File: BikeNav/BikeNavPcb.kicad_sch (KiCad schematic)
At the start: 3 parts, among them U1 TP4056, U2 ESP32-C3_SUPERMINI_TH

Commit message: Update PCB Design
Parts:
- added C1: 0.1 µF, Capacitor_THT:C_Disc_D10.0mm_W2.5mm_P5.00mm, symbol Device:C
- added J9: 1.8 TFT SPi 128x160 pins, Connector_PinSocket_2.54mm:PinSocket_1x08_P2.54mm_Vertical, symbol Connector:Conn_01x08_Pin
- added R1, R2: 100k, Resistor_THT:R_Axial_DIN0204_L3.6mm_D1.6mm_P5.08mm_Horizontal, symbol Device:R_US
- added SW1: SW_DPST_x2, Button_Switch_SMD:SW_DIP_SPSTx01_Slide_Copal_CHS-01A_W5.08mm_P1.27mm_JPin, symbol Switch:SW_DPST_x2
- added U3: 358, ST7735:ST7735, symbol ST7735:358
- U1: footprint Footprint:TP4056 -> TP4056:TP4056
- U2: footprint ESP32-C3_SUPERMINI_TH:MODULE_ESP32-C3_SUPERMINI_TH -> ESP32C3_Supermini_symbol_footprint:MODULE_ESP32-C3_SUPERMINI_TH
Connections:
- net BACKLIGHT: now also J9.1 (Pin_1), U3.1 (LITE)
- net OUT+: now also J9.8 (Pin_8), R1.2, SW1.2 (B), U3.9 (VCC); no longer U1.3 (OUT+)
- net OUT-: now also J9.7 (Pin_7), R2.2, U3.10 (GND)
- net BATT EST: now reaches U2.0 (GPIO0)
- net BATT EST: now also C1.1, R1.1
- net A0: now reaches U2.2 (GPIO2)
- net A0: now also J9.4 (Pin_4), U3.7 (D/C)
- net RESET: now reaches U2.3 (GPIO3)
- net RESET: now also J9.5 (Pin_5), U3.8 (RESET)
- net SCK: now reaches U2.4 (GPIO4)
- net SCK: now also J9.2 (Pin_2), U3.3 (SCK)
- net SDA: now reaches U2.6 (GPIO6)
- net SDA: now also J9.3 (Pin_3), U3.4 (MOSI)
- net CS: now reaches U2.7 (GPIO7)
- net CS: now also J9.6 (Pin_6), U3.5 (TFT_CS)
- new net: SW1.1 (A), U1.3 (OUT+)
- new net: C1.2, R2.1
- no-connect marks 0 -> 9
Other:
- note added: "1.8 TFT SPI 128*160 Display"
- note added: "Battery Charge Estimation Voltage Divider Circuit"
- note added: "Li ion Battery Charger and MCU Supply Voltage"
- note added: "Microcontroller unit"
- note added: "TFT Display Horizontal Pins Connector"
- moved on the sheet: BT1, U1, U2

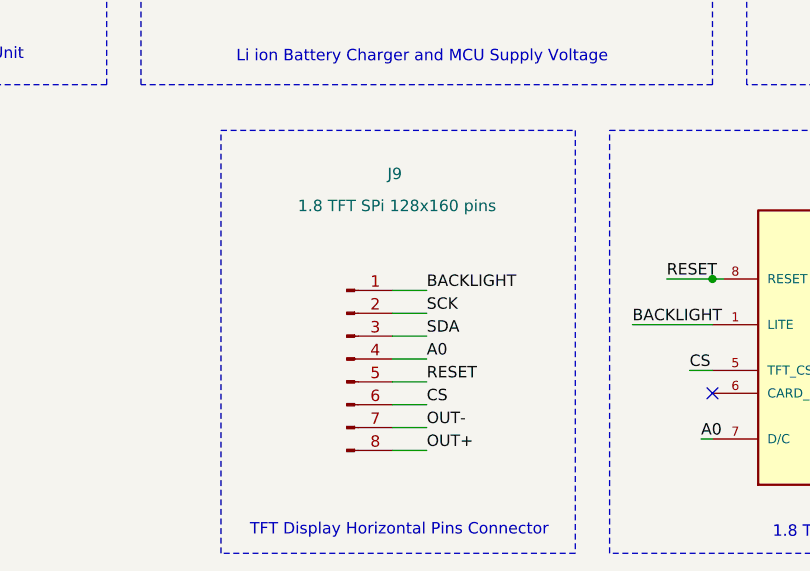
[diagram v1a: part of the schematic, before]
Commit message: Added Accurate dimesnsions for TFT mounting Holes and general optimization for Route Tracks.
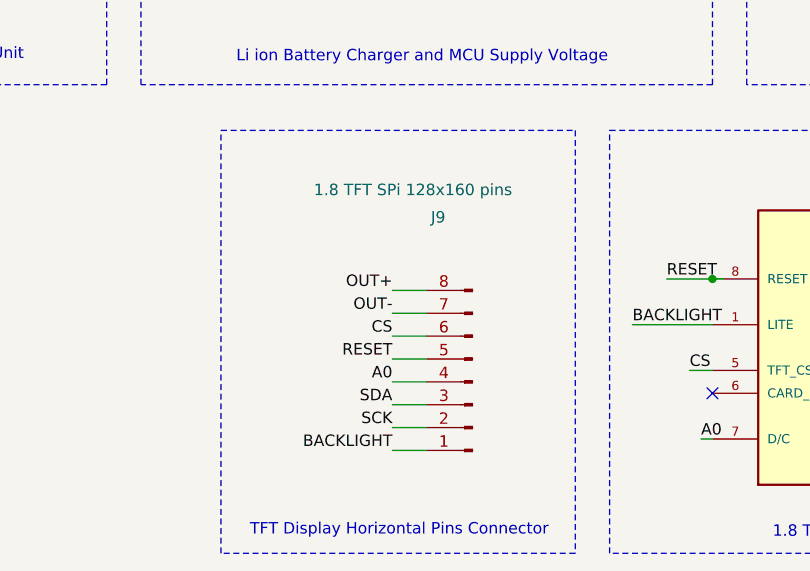
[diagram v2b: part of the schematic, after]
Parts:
- J9: footprint Connector_PinSocket_2.54mm:PinSocket_1x08_P2.54mm_Vertical -> Connector_PinHeader_2.54mm:PinHeader_1x08_P2.54mm_Vertical
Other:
- moved on the sheet: J9
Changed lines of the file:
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@@
 	(wire
 		(pts
-			(xy 114.3 115.57) (xy 110.49 115.57)
+			(xy 110.49 133.35) (xy 114.3 133.35)
 		)
 		(stroke
@@
 	(wire
 		(pts
-			(xy 114.3 120.65) (xy 110.49 120.65)
+			(xy 110.49 128.27) (xy 114.3 128.27)
 		)
 		(stroke
@@
 	(wire
 		(pts
-			(xy 114.3 130.81) (xy 110.49 130.81)
+			(xy 110.49 118.11) (xy 114.3 118.11)
 		)
 		(stroke
@@
 	(wire
 		(pts
-			(xy 114.3 133.35) (xy 110.49 133.35)
-		)
-		(stroke
-			(width 0)
-			(type default)
-		)
-	)
-	(wire
-		(pts
-			(xy 114.3 123.19) (xy 110.49 123.19)
+			(xy 110.49 115.57) (xy 114.3 115.57)
+		)
+		(stroke
+			(width 0)
+			(type default)
+		)
+	)
+	(wire
+		(pts
+			(xy 110.49 125.73) (xy 114.3 125.73)
 		)
 		(stroke
@@
 	(wire
 		(pts
-			(xy 114.3 128.27) (xy 110.49 128.27)
+			(xy 110.49 120.65) (xy 114.3 120.65)
 		)
 		(stroke
@@
 	(wire
 		(pts
-			(xy 114.3 118.11) (xy 110.49 118.11)
+			(xy 110.49 130.81) (xy 114.3 130.81)
 		)
 		(stroke
@@
 	(wire
 		(pts
-			(xy 114.3 125.73) (xy 110.49 125.73)
+			(xy 110.49 123.19) (xy 114.3 123.19)
 		)
 		(stroke
@@
 	)
 	(label "SCK"
-		(at 114.3 118.11 0)
-		(effects
-			(font
-				(size 1.27 1.27)
-			)
-			(justify left bottom)
+		(at 110.49 130.81 180)
+		(effects
+			(font
+				(size 1.27 1.27)
+			)
+			(justify right bottom)
 		)
 	)
 	(label "SDA"
-		(at 114.3 120.65 0)
-		(effects
-			(font
-				(size 1.27 1.27)
-			)
-			(justify left bottom)
+		(at 110.49 128.27 180)
+		(effects
+			(font
+				(size 1.27 1.27)
+			)
+			(justify right bottom)
 		)
 	)
@@
 	)
 	(label "A0"
-		(at 114.3 123.19 0)
-		(effects
-			(font
-				(size 1.27 1.27)
-			)
-			(justify left bottom)
+		(at 110.49 125.73 180)
+		(effects
+			(font
+				(size 1.27 1.27)
+			)
+			(justify right bottom)
 		)
 	)
@@
 	)
 	(label "CS"
-		(at 114.3 128.27 0)
-		(effects
-			(font
-				(size 1.27 1.27)
-			)
-			(justify left bottom)
+		(at 110.49 120.65 180)
+		(effects
+			(font
+				(size 1.27 1.27)
+			)
+			(justify right bottom)
 		)
 	)
@@
 	)
 	(label "OUT-"
-		(at 114.3 130.81 0)
-		(effects
-			(font
-				(size 1.27 1.27)
-			)
-			(justify left bottom)
+		(at 110.49 118.11 180)
+		(effects
+			(font
+				(size 1.27 1.27)
+			)
+			(justify right bottom)
 		)
 	)
 	(label "BACKLIGHT"
-		(at 114.3 115.57 0)
-		(effects
-			(font
-				(size 1.27 1.27)
-			)
-			(justify left bottom)
+		(at 110.49 133.35 180)
+		(effects
+			(font
+				(size 1.27 1.27)
+			)
+			(justify right bottom)
 		)
 	)
 	(label "RESET"
-		(at 114.3 125.73 0)
-		(effects
-			(font
-				(size 1.27 1.27)
-			)
-			(justify left bottom)
+		(at 110.49 123.19 180)
+		(effects
+			(font
+				(size 1.27 1.27)
+			)
+			(justify right bottom)
 		)
 	)
 	(label "OUT+"
-		(at 114.3 133.35 0)
-		(effects
-			(font
-				(size 1.27 1.27)
-			)
-			(justify left bottom)
+		(at 110.49 115.57 180)
+		(effects
+			(font
+				(size 1.27 1.27)
+			)
+			(justify right bottom)
 		)
 	)
 	(symbol
 		(lib_id "Connector:Conn_01x08_Pin")
-		(at 105.41 123.19 0)
+		(at 119.38 125.73 180)
 		(unit 1)
 		(body_style 1)
@@
 		(dnp no)
 		(property "Reference" "J9"
-			(at 110.744 102.616 0)
+			(at 115.57 107.442 0)
 			(show_name no)
 			(do_not_autoplace no)
@@
 		)
 		(property "Value" "1.8 TFT SPi 128x160 pins"
-			(at 110.998 106.172 0)
+			(at 112.776 104.394 0)
 			(show_name no)
 			(do_not_autoplace no)
@@
 			)
 		)
-		(property "Footprint" "Connector_PinSocket_2.54mm:PinSocket_1x08_P2.54mm_Vertical"
-			(at 105.41 123.19 0)
+		(property "Footprint" "Connector_PinHeader_2.54mm:PinHeader_1x08_P2.54mm_Vertical"
+			(at 119.38 125.73 0)
 			(hide yes)
 			(show_name no)
@@
 		)
 		(property "Datasheet" ""
-			(at 105.41 123.19 0)
+			(at 119.38 125.73 0)
 			(hide yes)
 			(show_name no)
@@
 		)
 		(property "Description" "Generic connector, single row, 01x08, script generated"
-			(at 105.41 123.19 0)
+			(at 119.38 125.73 0)
 			(hide yes)
 			(show_name no)

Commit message: Added Accurate Dimension for TFT Display Mounting Holes and Step File for it.
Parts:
- J9: footprint Connector_PinHeader_2.54mm:PinHeader_1x08_P2.54mm_Vertical -> Connector_PinSocket_2.54mm:PinSocket_1x08_P2.54mm_Vertical
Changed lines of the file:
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@@
 			)
 		)
-		(property "Footprint" "Connector_PinHeader_2.54mm:PinHeader_1x08_P2.54mm_Vertical"
+		(property "Footprint" "Connector_PinSocket_2.54mm:PinSocket_1x08_P2.54mm_Vertical"
 			(at 119.38 125.73 0)
 			(hide yes)

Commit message: Added New Compact Footprint for THT Capacitor and 3d Model.
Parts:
- C1: footprint Capacitor_THT:C_Disc_D10.0mm_W2.5mm_P5.00mm -> Capacitor_THT:C_Disc_D3.0mm_W1.6mm_P2.50mm
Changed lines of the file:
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@@
 			)
 		)
-		(property "Footprint" "Capacitor_THT:C_Disc_D10.0mm_W2.5mm_P5.00mm"
+		(property "Footprint" "Capacitor_THT:C_Disc_D3.0mm_W1.6mm_P2.50mm"
 			(at 171.1452 68.58 0)
 			(hide yes)
